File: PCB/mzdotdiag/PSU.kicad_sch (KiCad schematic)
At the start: 8 parts

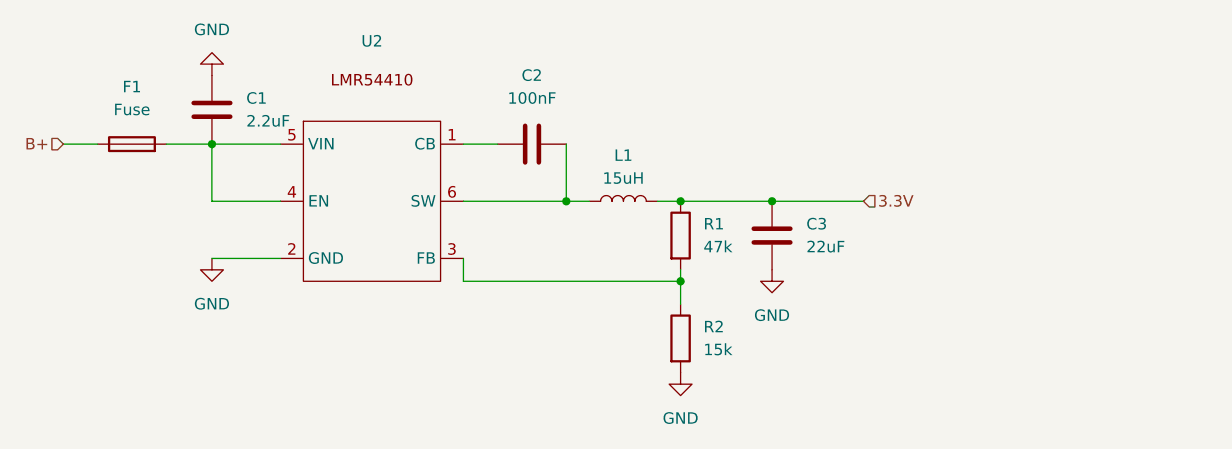
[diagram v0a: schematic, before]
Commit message: Lots of schematic updates, found CD4504B for logic level shifting
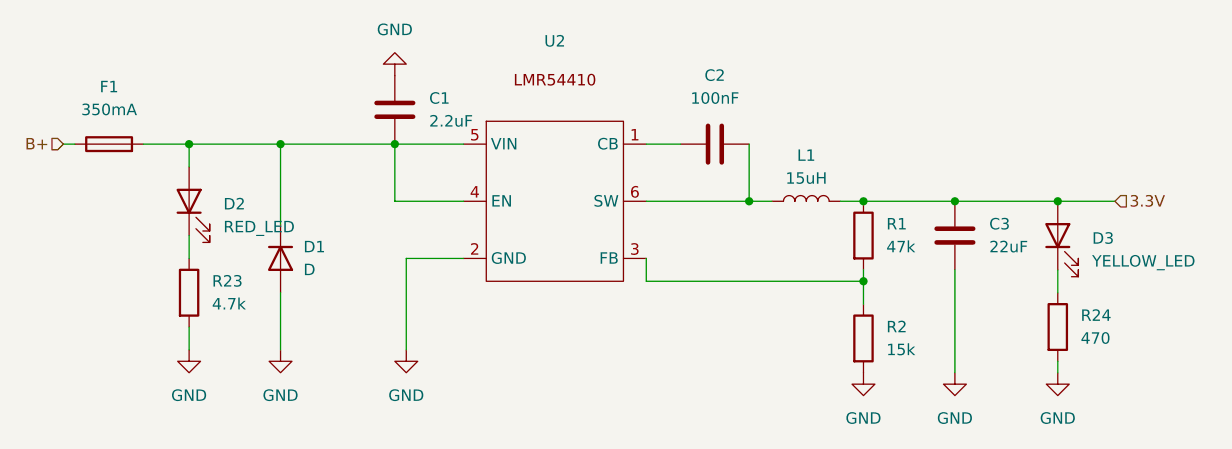
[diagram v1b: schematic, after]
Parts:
- added D1: D, Diode_SMD:D_SMB, symbol Device:D
- added D2: RED_LED, LED_SMD:LED_0805_2012Metric, symbol Device:LED
- added D3: YELLOW_LED, LED_SMD:LED_0805_2012Metric, symbol Device:LED
- added R23: 4.7k, Resistor_SMD:R_0603_1608Metric_Pad0.98x0.95mm_HandSolder, symbol Device:R
- added R24: 470, Resistor_SMD:R_0603_1608Metric_Pad0.98x0.95mm_HandSolder, symbol Device:R
- C1: footprint (none) -> Capacitor_SMD:C_0805_2012Metric; LOMEX (none) -> 82-08-18
- C2: footprint (none) -> Capacitor_SMD:C_0805_2012Metric; LOMEX (none) -> 82-13-46
- C3: footprint (none) -> Capacitor_SMD:C_1210_3225Metric_Pad1.33x2.70mm_HandSolder; LOMEX (none) -> 82-07-04
- F1: value Fuse -> 350mA; footprint (none) -> Fuse:Fuse_1812_4532Metric_Pad1.30x3.40mm_HandSolder; LOMEX (none) -> 44-04-70
- L1: footprint (none) -> Inductor_SMD:L_Coilcraft_MSS7348-XXX; LOMEX (none) -> 93-04-10
- R1: footprint (none) -> Resistor_SMD:R_0603_1608Metric_Pad0.98x0.95mm_HandSolder; LOMEX (none) -> 80-11-72
- R2: footprint (none) -> Resistor_SMD:R_0603_1608Metric_Pad0.98x0.95mm_HandSolder; LOMEX (none) -> 80-12-06
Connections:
- net 3.3V: now also D3.2 (A)
- net GND: now also D1.2 (A), R23.2, R24.2
- net at C1.2, F1.2, U2.4 (EN)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: now also D1.1 (K), D2.2 (A)
- new net: D2.1 (K), R23.1
- new net: D3.1 (K), R24.1
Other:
- moved on the sheet: C1, C2, C3, F1, L1, R1, R2, U2

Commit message: schematic and pcb update with new levelshifter IC
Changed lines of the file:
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@@
 (kicad_sch
-	(version 20231120)
+	(version 20250114)
 	(generator "eeschema")
-	(generator_version "8.0")
+	(generator_version "9.0")
 	(paper "A4")
 	(junction
@@
 		(shape input)
 		(at 26.67 33.02 180)
-		(fields_autoplaced yes)
 		(effects
 			(font
@@
 		(shape input)
 		(at 143.51 39.37 0)
-		(fields_autoplaced yes)
 		(effects
 			(font

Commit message: finished wiring
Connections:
- net B+_PROT: now reaches C1.2, D1.1 (K), D2.2 (A), F1.2, U2.4 (EN), U2.5 (VIN)
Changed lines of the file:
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@@
+		)
+	)
+	(hierarchical_label "B+_PROT"
+		(shape input)
+		(at 50.8 33.02 90)
+		(effects
+			(font
+				(size 1.27 1.27)
+			)
+			(justify left)
 		)
 	)
